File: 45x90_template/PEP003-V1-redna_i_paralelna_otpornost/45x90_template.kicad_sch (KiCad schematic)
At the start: 23 parts, among them J1 Screw_Terminal_01x02

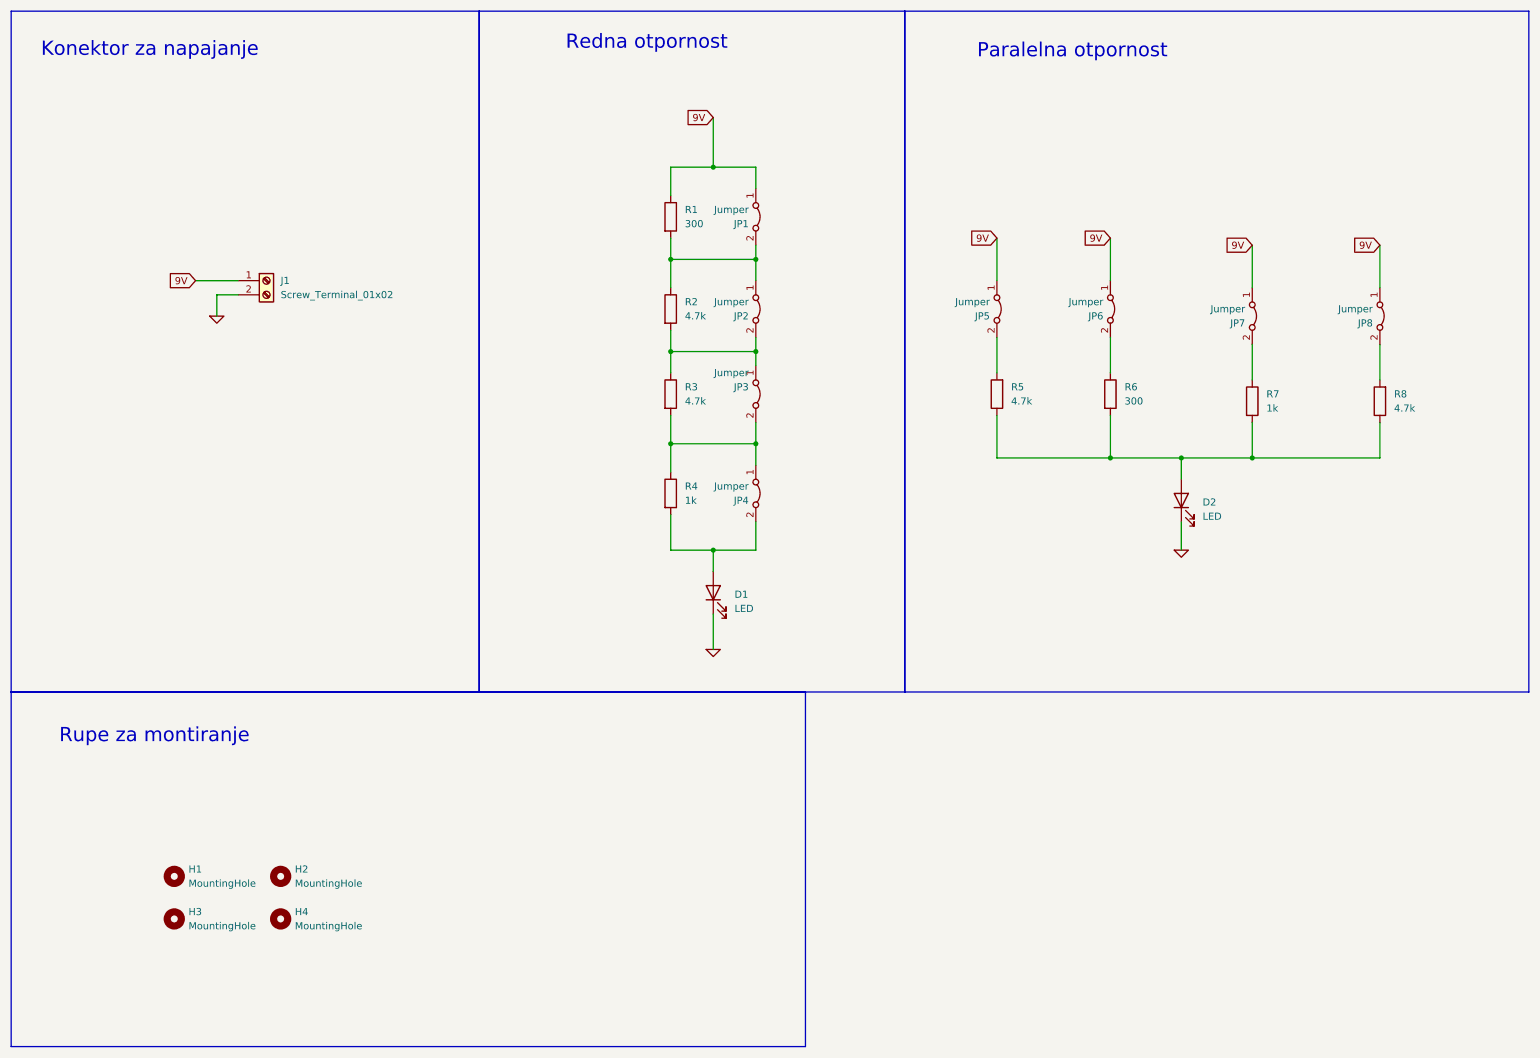
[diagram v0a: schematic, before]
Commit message: PEP004 and template 90 update.
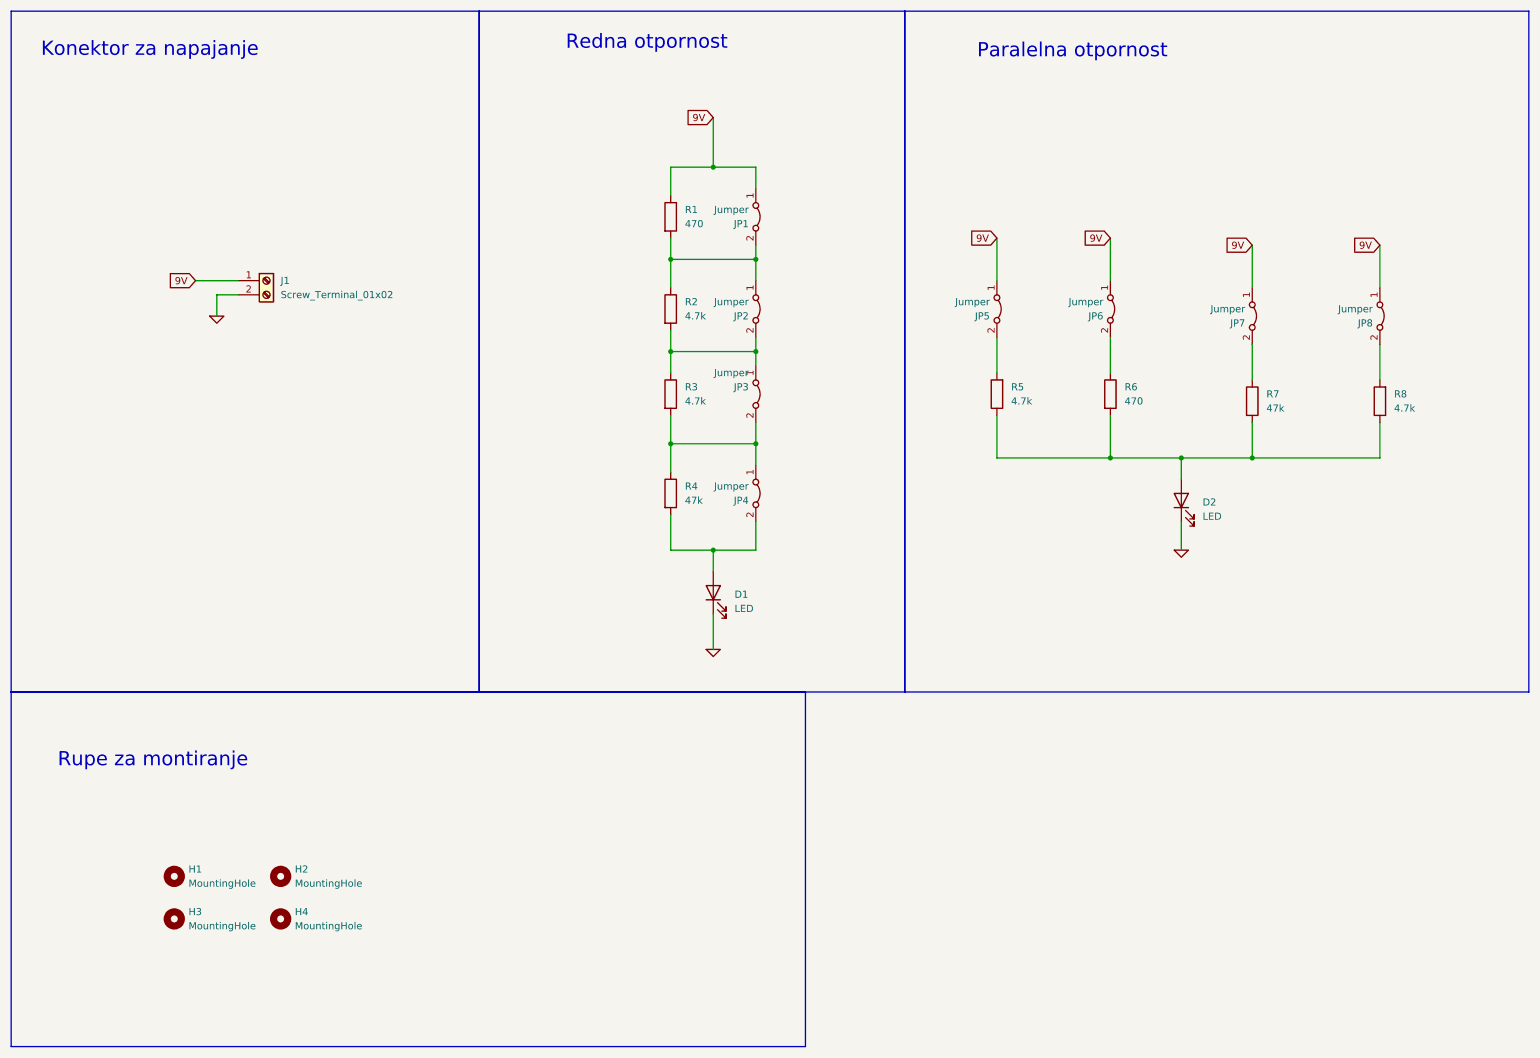
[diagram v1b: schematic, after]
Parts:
- D1, D2: footprint LED_SMD:LED_0603_1608Metric_Pad1.05x0.95mm_HandSolder -> LED_SMD:LED_1206_3216Metric_Pad1.42x1.75mm_HandSolder
- J1: footprint PEP_library:TerminalBlock_Phoenix_MKDS-1,5-2-5.08_1x02_P5.08mm_Horizontal -> TerminalBlock_Phoenix:TerminalBlock_Phoenix_MKDS-1,5-2-5.08_1x02_P5.08mm_Horizontal
- R1, R6: value 300 -> 470; footprint PEP_library:R_smd -> Resistor_SMD:R_1206_3216Metric_Pad1.30x1.75mm_HandSolder
- R2, R3, R5, R8: footprint PEP_library:R_smd -> Resistor_SMD:R_1206_3216Metric_Pad1.30x1.75mm_HandSolder
- R4, R7: value 1k -> 47k; footprint PEP_library:R_smd -> Resistor_SMD:R_1206_3216Metric_Pad1.30x1.75mm_HandSolder
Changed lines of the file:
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@@
 			(width 0)
 			(type default)
+			(color 110 183 49 1)
 		)
 		(fill
@@
 			(width 0)
 			(type default)
+			(color 110 183 49 1)
 		)
 		(fill
@@
 			(width 0)
 			(type default)
+			(color 110 183 49 1)
 		)
 		(fill
@@
 			(width 0)
 			(type default)
+			(color 110 183 49 1)
 		)
 		(fill
@@
 			(font
 				(size 2.54 2.54)
+				(color 110 183 49 1)
 			)
 			(justify left bottom)
@@
 	(text "Rupe za montiranje"
 		(exclude_from_sim no)
-		(at 38.354 142.494 0)
+		(at 38.1 146.812 0)
 		(effects
 			(font
 				(size 2.54 2.54)
+				(color 110 183 49 1)
 			)
 		)
@@
 			(font
 				(size 2.54 2.54)
+				(color 110 183 49 1)
 			)
 			(justify left bottom)
@@
 			(font
 				(size 2.54 2.54)
+				(color 110 183 49 1)
 			)
 			(justify left bottom)
@@
 			)
 		)
-		(property "Footprint" "PEP_library:R_smd"
+		(property "Footprint" "Resistor_SMD:R_1206_3216Metric_Pad1.30x1.75mm_HandSolder"
 			(at 129.032 81.28 90)
 			(effects
@@
 			)
 		)
-		(property "Value" "300"
+		(property "Value" "470"
 			(at 133.35 50.8 0)
 			(effects
@@
 			)
 		)
-		(property "Footprint" "PEP_library:R_smd"
+		(property "Footprint" "Resistor_SMD:R_1206_3216Metric_Pad1.30x1.75mm_HandSolder"
 			(at 129.032 49.53 90)
 			(effects
@@
 			)
 		)
-		(property "Footprint" "PEP_library:R_smd"
+		(property "Footprint" "Resistor_SMD:R_1206_3216Metric_Pad1.30x1.75mm_HandSolder"
 			(at 191.008 81.28 90)
 			(effects
@@
 			)
 		)
-		(property "Footprint" "LED_SMD:LED_0603_1608Metric_Pad1.05x0.95mm_HandSolder"
+		(property "Footprint" "LED_SMD:LED_1206_3216Metric_Pad1.42x1.75mm_HandSolder"
 			(at 222.25 100.33 0)
 			(effects
@@
 			)
 		)
-		(property "Footprint" "PEP_library:R_smd"
+		(property "Footprint" "Resistor_SMD:R_1206_3216Metric_Pad1.30x1.75mm_HandSolder"
 			(at 259.588 82.55 90)
 			(effects
@@
 			)
 		)
-		(property "Value" "300"
+		(property "Value" "470"
 			(at 212.09 82.55 0)
 			(effects
@@
 			)
 		)
-		(property "Footprint" "PEP_library:R_smd"
+		(property "Footprint" "Resistor_SMD:R_1206_3216Metric_Pad1.30x1.75mm_HandSolder"
 			(at 207.772 81.28 90)
 			(effects
@@
 			)
 		)
-		(property "Footprint" "LED_SMD:LED_0603_1608Metric_Pad1.05x0.95mm_HandSolder"
+		(property "Footprint" "LED_SMD:LED_1206_3216Metric_Pad1.42x1.75mm_HandSolder"
 			(at 138.43 116.84 0)
 			(effects
@@
 			)
 		)
-		(property "Value" "1k"
+		(property "Value" "47k"
 			(at 237.49 83.82 0)
 			(effects
@@
 			)
 		)
-		(property "Footprint" "PEP_library:R_smd"
+		(property "Footprint" "Resistor_SMD:R_1206_3216Metric_Pad1.30x1.75mm_HandSolder"
 			(at 233.172 82.55 90)
 			(effects
@@
 			)
 		)
-		(property "Footprint" "PEP_library:R_smd"
+		(property "Footprint" "Resistor_SMD:R_1206_3216Metric_Pad1.30x1.75mm_HandSolder"
 			(at 129.032 66.04 90)
 			(effects
@@
 			)
 		)
-		(property "Footprint" "PEP_library:TerminalBlock_Phoenix_MKDS-1,5-2-5.08_1x02_P5.08mm_Horizontal"
+		(property "Footprint" "TerminalBlock_Phoenix:TerminalBlock_Phoenix_MKDS-1,5-2-5.08_1x02_P5.08mm_Horizontal"
 			(at 58.42 60.96 0)
 			(effects
@@
 			)
 		)
-		(property "Value" "1k"
+		(property "Value" "47k"
 			(at 133.35 100.3299 0)
 			(effects
@@
 			)
 		)
-		(property "Footprint" "PEP_library:R_smd"
+		(property "Footprint" "Resistor_SMD:R_1206_3216Metric_Pad1.30x1.75mm_HandSolder"
 			(at 129.032 99.06 90)
 			(effects
